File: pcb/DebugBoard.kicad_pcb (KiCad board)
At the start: 4 copper layers, 40 x 40 mm, 4 parts

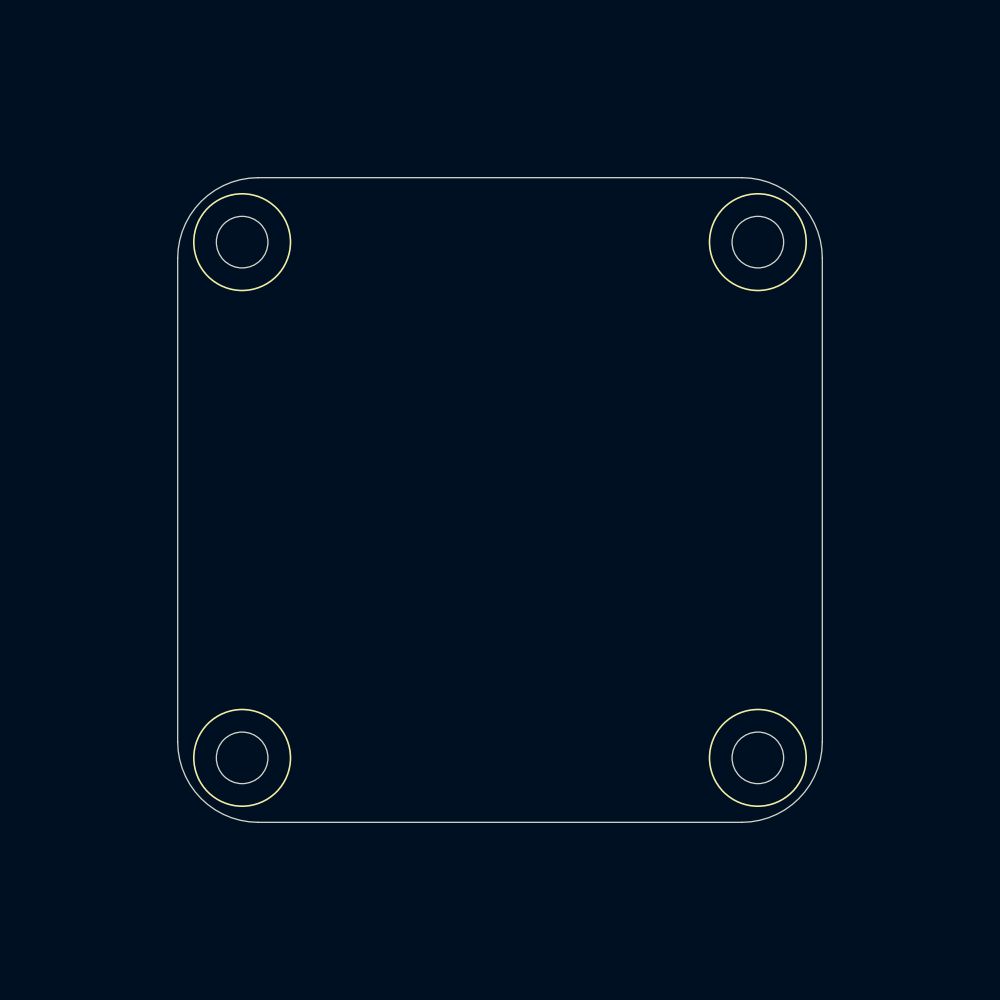
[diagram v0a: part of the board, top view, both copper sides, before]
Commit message: Basic expected components for `DebugBoard` PCB.
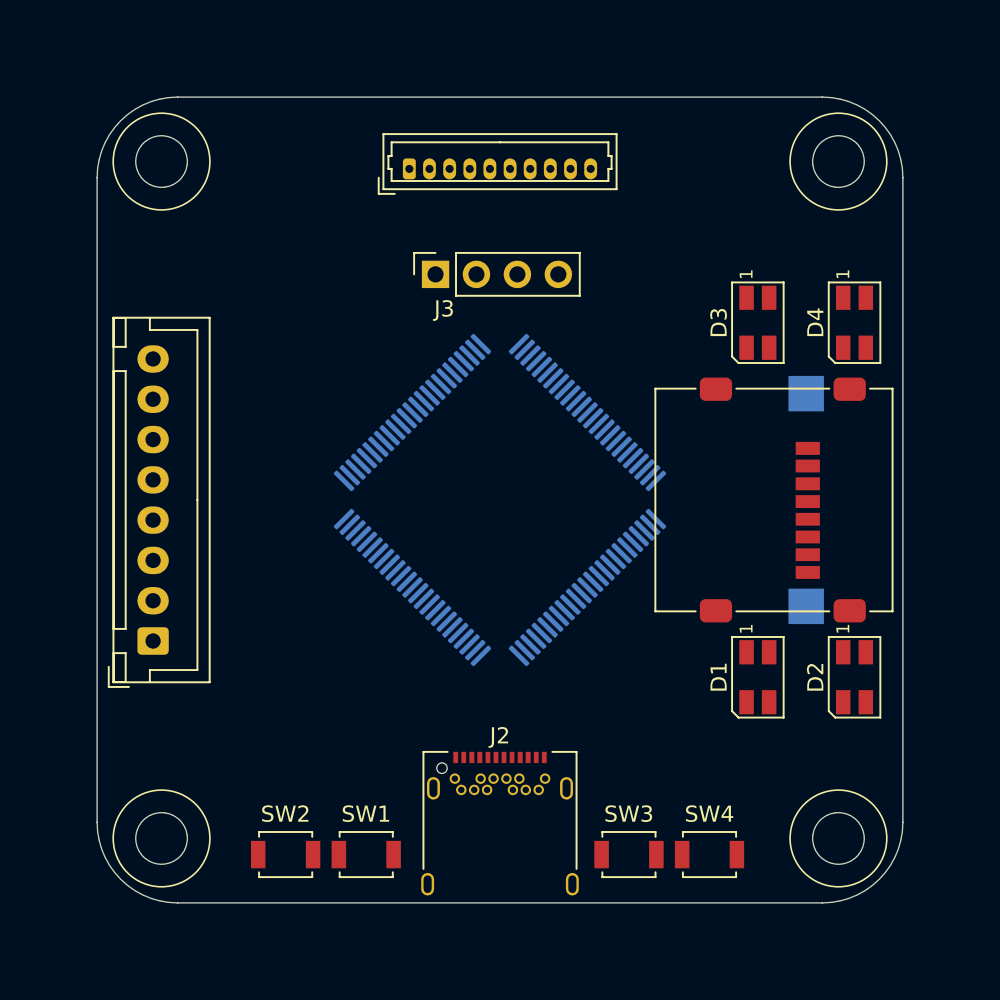
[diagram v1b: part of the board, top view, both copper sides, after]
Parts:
- added BZ1: AST1109MLTRQ, Buzzer_Beeper:Buzzer_Mallory_AST1109MLTRQ, B.Cu at (169.0, 100.0)
- added D1: 150141M173100, LED_SMD:LED_RGB_Wuerth-PLCC4_3.2x2.8mm_150141M173100, F.Cu at (166.0, 111.0)
- added D2: 150141M173100, LED_SMD:LED_RGB_Wuerth-PLCC4_3.2x2.8mm_150141M173100, F.Cu at (172.0, 111.0)
- added D3: 150141M173100, LED_SMD:LED_RGB_Wuerth-PLCC4_3.2x2.8mm_150141M173100, F.Cu at (166.0, 89.0)
- added D4: 150141M173100, LED_SMD:LED_RGB_Wuerth-PLCC4_3.2x2.8mm_150141M173100, F.Cu at (172.0, 89.0)
- added J1: Debug, pcb:Molex_PicoBlade_53047-1010_1x10_P1.25mm_Vertical, F.Cu at (144.4, 79.5)
- added J2: USB_C_Receptacle, pcb:USB_C_Receptacle_Amphenol_12401548E4-2A, F.Cu at (150.0, 121.0)
- added J3: Conn_01x04, pcb:SSD1306_Module_Connector, F.Cu at (146.0, 86.0)
- added J4: B8B-XH-A, Connector_JST:JST_XH_B8B-XH-A_1x08_P2.50mm_Vertical, F.Cu at (128.5, 108.8)
- added J5: 0472192001, pcb:microSD_HC_Molex_47219-2001, F.Cu at (167.0, 100.0)
- added SW1: B3U-1000P, Button_Switch_SMD:SW_SPST_B3U-1000P, F.Cu at (141.7, 122.0)
- added SW2: B3U-1000P, Button_Switch_SMD:SW_SPST_B3U-1000P, F.Cu at (136.7, 122.0)
- added SW3: B3U-1000P, Button_Switch_SMD:SW_SPST_B3U-1000P, F.Cu at (158.0, 122.0)
- added SW4: B3U-1000P, Button_Switch_SMD:SW_SPST_B3U-1000P, F.Cu at (163.0, 122.0)
- added U1: STM32H533VET6, Package_QFP:LQFP-100_14x14mm_P0.5mm, B.Cu at (150.0, 100.0)
- moved H1 7.07 mm to (129.0, 121.0)
- moved H2 7.07 mm to (171.0, 79.0)
- moved H3 7.07 mm to (129.0, 79.0)
- moved H4 7.07 mm to (171.0, 121.0)
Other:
- board size 40 x 40 mm -> 50 x 50 mm

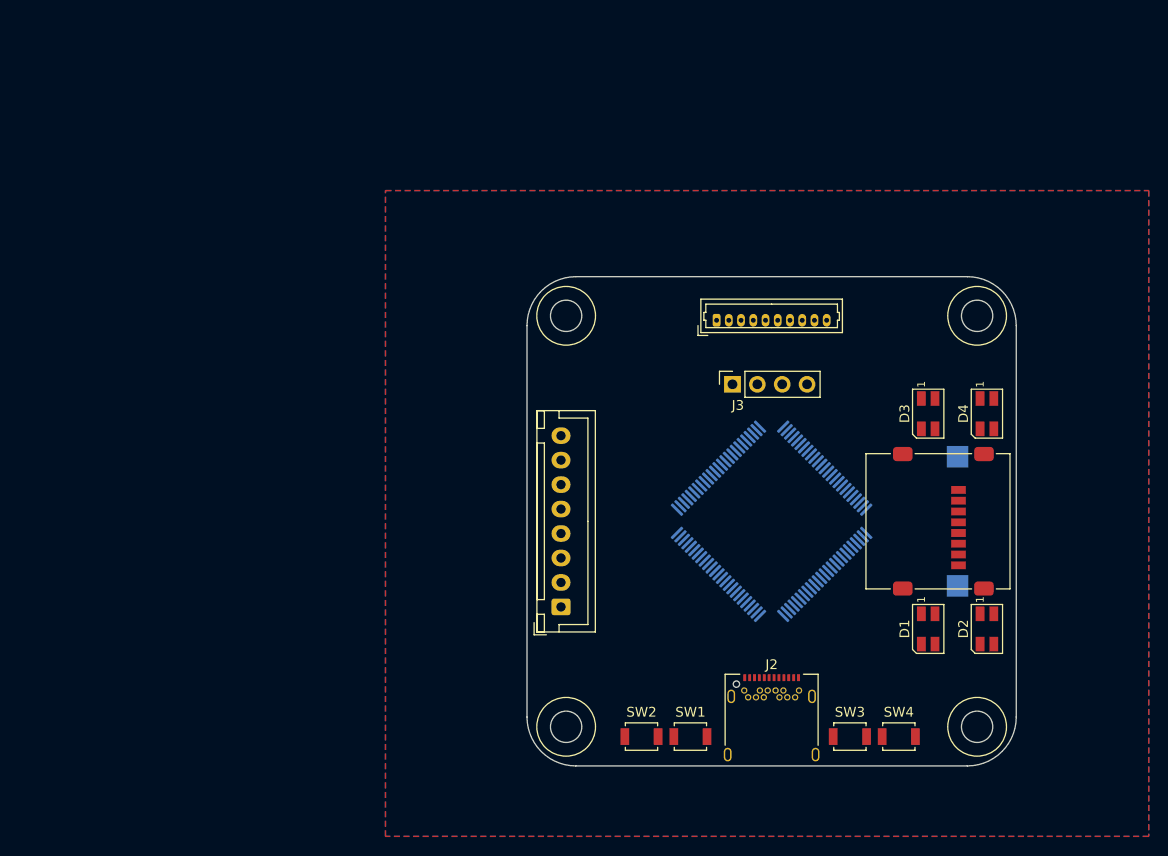
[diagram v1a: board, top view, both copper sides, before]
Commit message: Worked out uSD connector and debug LEDs details for `DebugBoard`.
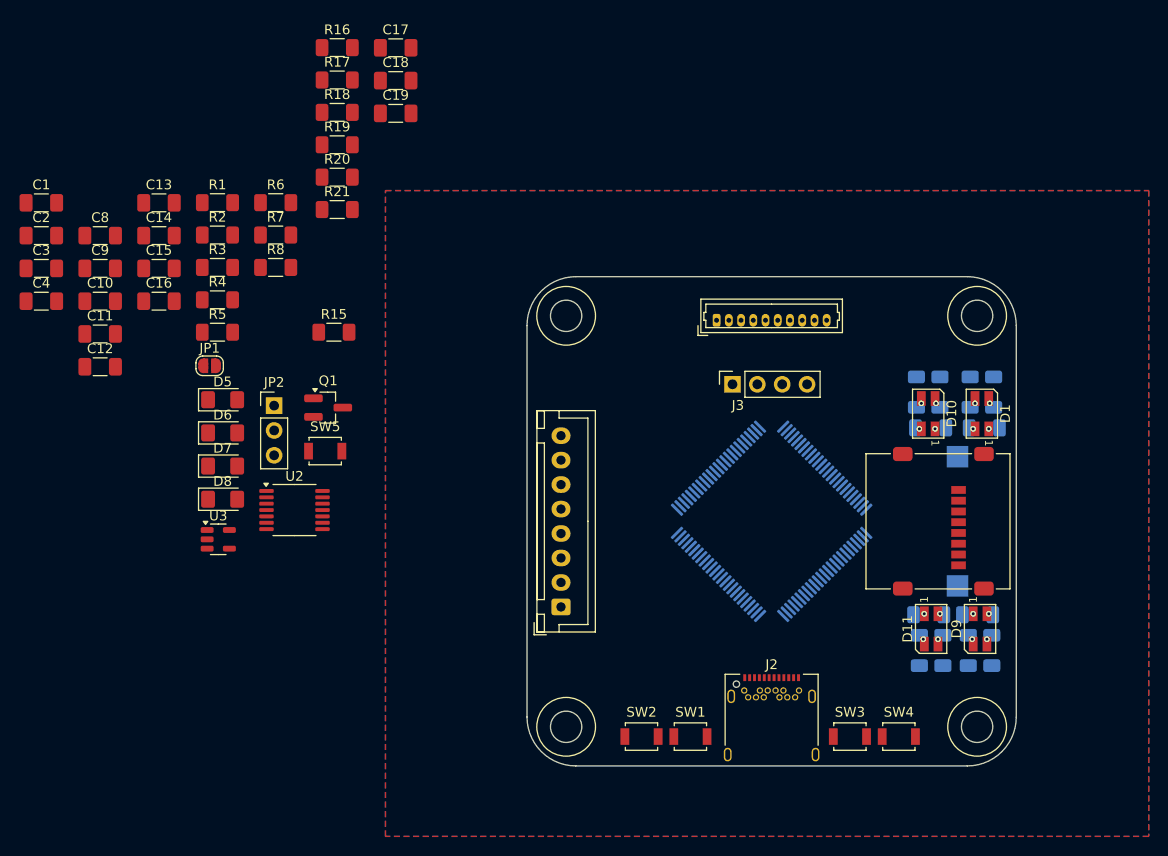
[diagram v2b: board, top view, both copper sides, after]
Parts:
- removed D2, D3, D4: 150141M173100, LED_SMD:LED_RGB_Wuerth-PLCC4_3.2x2.8mm_150141M173100
- added C1: 10u, Capacitor_SMD:C_1206_3216Metric_Pad1.33x1.80mm_HandSolder, F.Cu at (75.4, 67.5)
- added C10: 100n, Capacitor_SMD:C_1206_3216Metric_Pad1.33x1.80mm_HandSolder, F.Cu at (81.4, 77.5)
- added C11: 100n, Capacitor_SMD:C_1206_3216Metric_Pad1.33x1.80mm_HandSolder, F.Cu at (81.4, 80.9)
- added C12: 100n, Capacitor_SMD:C_1206_3216Metric_Pad1.33x1.80mm_HandSolder, F.Cu at (81.4, 84.2)
- added C13: 100n, Capacitor_SMD:C_1206_3216Metric_Pad1.33x1.80mm_HandSolder, F.Cu at (87.4, 67.5)
- added C14: 100n, Capacitor_SMD:C_1206_3216Metric_Pad1.33x1.80mm_HandSolder, F.Cu at (87.4, 70.8)
- added C15: 2u2, Capacitor_SMD:C_1206_3216Metric_Pad1.33x1.80mm_HandSolder, F.Cu at (87.4, 74.2)
- added C16: 2u2, Capacitor_SMD:C_1206_3216Metric_Pad1.33x1.80mm_HandSolder, F.Cu at (87.4, 77.5)
- added C17: 1u, Capacitor_SMD:C_1206_3216Metric_Pad1.33x1.80mm_HandSolder, F.Cu at (111.6, 51.6)
- added C18: 100n, Capacitor_SMD:C_1206_3216Metric_Pad1.33x1.80mm_HandSolder, F.Cu at (111.6, 55.0)
- added C19: 10n, Capacitor_SMD:C_1206_3216Metric_Pad1.33x1.80mm_HandSolder, F.Cu at (111.6, 58.3)
- added C2: 1u, Capacitor_SMD:C_1206_3216Metric_Pad1.33x1.80mm_HandSolder, F.Cu at (75.4, 70.8)
- added C3: 1u, Capacitor_SMD:C_1206_3216Metric_Pad1.33x1.80mm_HandSolder, F.Cu at (75.4, 74.2)
- added C4: 100n, Capacitor_SMD:C_1206_3216Metric_Pad1.33x1.80mm_HandSolder, F.Cu at (75.4, 77.5)
- added C8: 4u7, Capacitor_SMD:C_1206_3216Metric_Pad1.33x1.80mm_HandSolder, F.Cu at (81.4, 70.8)
- added C9: 100n, Capacitor_SMD:C_1206_3216Metric_Pad1.33x1.80mm_HandSolder, F.Cu at (81.4, 74.2)
- added D10: 150141M173100, LED_SMD:LED_RGB_Wuerth-PLCC4_3.2x2.8mm_150141M173100, F.Cu at (166.0, 89.0)
- added D11: 150141M173100, LED_SMD:LED_RGB_Wuerth-PLCC4_3.2x2.8mm_150141M173100, F.Cu at (166.3, 111.0)
- added D5: GREEN, LED_SMD:LED_1206_3216Metric_Pad1.42x1.75mm_HandSolder, F.Cu at (93.9, 87.6)
- added D6: GREEN, LED_SMD:LED_1206_3216Metric_Pad1.42x1.75mm_HandSolder, F.Cu at (93.9, 91.0)
- added D7: RED, LED_SMD:LED_1206_3216Metric_Pad1.42x1.75mm_HandSolder, F.Cu at (93.9, 94.4)
- added D8: GREEN, LED_SMD:LED_1206_3216Metric_Pad1.42x1.75mm_HandSolder, F.Cu at (93.9, 97.7)
- added D9: 150141M173100, LED_SMD:LED_RGB_Wuerth-PLCC4_3.2x2.8mm_150141M173100, F.Cu at (171.3, 111.0)
- added JP1: SolderJumper_2_Open, Jumper:SolderJumper-2_P1.3mm_Open_RoundedPad1.0x1.5mm, F.Cu at (92.6, 84.1)
- added JP2: Jumper_3_Bridged12, Connector_PinHeader_2.54mm:PinHeader_1x03_P2.54mm_Vertical, F.Cu at (99.2, 88.2)
- added Q1: S8050, Package_TO_SOT_SMD:SOT-23_Handsoldering, F.Cu at (104.7, 88.4)
- added R1: 5k1, Resistor_SMD:R_1206_3216Metric_Pad1.30x1.75mm_HandSolder, F.Cu at (93.4, 67.4)
- added R10: 6k8, Resistor_SMD:R_1206_3216Metric_Pad1.30x1.75mm_HandSolder, B.Cu at (170.3, 86.8)
- added R11: 6k8, Resistor_SMD:R_1206_3216Metric_Pad1.30x1.75mm_HandSolder, B.Cu at (171.7, 90.5)
- added R12: 6k8, Resistor_SMD:R_1206_3216Metric_Pad1.30x1.75mm_HandSolder, B.Cu at (170.1, 113.2)
- added R13: 6k8, Resistor_SMD:R_1206_3216Metric_Pad1.30x1.75mm_HandSolder, B.Cu at (172.5, 113.2)
- added R14: 6k8, Resistor_SMD:R_1206_3216Metric_Pad1.30x1.75mm_HandSolder, B.Cu at (171.0, 109.5)
- added R15: 47k, Resistor_SMD:R_1206_3216Metric_Pad1.30x1.75mm_HandSolder, F.Cu at (105.3, 80.7)
- added R16: R_Small, Resistor_SMD:R_1206_3216Metric_Pad1.30x1.75mm_HandSolder, F.Cu at (105.6, 51.6)
- added R17: R_Small, Resistor_SMD:R_1206_3216Metric_Pad1.30x1.75mm_HandSolder, F.Cu at (105.6, 54.9)
- added R18: R_Small, Resistor_SMD:R_1206_3216Metric_Pad1.30x1.75mm_HandSolder, F.Cu at (105.6, 58.2)
- added R19: R_Small, Resistor_SMD:R_1206_3216Metric_Pad1.30x1.75mm_HandSolder, F.Cu at (105.6, 61.5)
- added R2: 4K, Resistor_SMD:R_1206_3216Metric_Pad1.30x1.75mm_HandSolder, F.Cu at (93.4, 70.7)
- added R20: R_Small, Resistor_SMD:R_1206_3216Metric_Pad1.30x1.75mm_HandSolder, F.Cu at (105.6, 64.8)
- added R21: R_Small, Resistor_SMD:R_1206_3216Metric_Pad1.30x1.75mm_HandSolder, F.Cu at (105.6, 68.1)
- added R22: 6k8, Resistor_SMD:R_1206_3216Metric_Pad1.30x1.75mm_HandSolder, B.Cu at (167.2, 86.8)
- added R23: 6k8, Resistor_SMD:R_1206_3216Metric_Pad1.30x1.75mm_HandSolder, B.Cu at (164.8, 86.8)
- added R24: 6k8, Resistor_SMD:R_1206_3216Metric_Pad1.30x1.75mm_HandSolder, B.Cu at (166.3, 90.5)
- added R25: 6k8, Resistor_SMD:R_1206_3216Metric_Pad1.30x1.75mm_HandSolder, B.Cu at (165.1, 113.2)
- added R26: 6k8, Resistor_SMD:R_1206_3216Metric_Pad1.30x1.75mm_HandSolder, B.Cu at (167.5, 113.2)
- added R27: 6k8, Resistor_SMD:R_1206_3216Metric_Pad1.30x1.75mm_HandSolder, B.Cu at (166.0, 109.5)
- added R3: 10K, Resistor_SMD:R_1206_3216Metric_Pad1.30x1.75mm_HandSolder, F.Cu at (93.4, 74.1)
- added R4: 4K, Resistor_SMD:R_1206_3216Metric_Pad1.30x1.75mm_HandSolder, F.Cu at (93.4, 77.4)
- added R5: 2K, Resistor_SMD:R_1206_3216Metric_Pad1.30x1.75mm_HandSolder, F.Cu at (93.4, 80.7)
- added R6: 2K, Resistor_SMD:R_1206_3216Metric_Pad1.30x1.75mm_HandSolder, F.Cu at (99.3, 67.4)
- added R7: 50k, Resistor_SMD:R_1206_3216Metric_Pad1.30x1.75mm_HandSolder, F.Cu at (99.3, 70.7)
- added R8: 10k, Resistor_SMD:R_1206_3216Metric_Pad1.30x1.75mm_HandSolder, F.Cu at (99.3, 74.1)
- added R9: 6k8, Resistor_SMD:R_1206_3216Metric_Pad1.30x1.75mm_HandSolder, B.Cu at (172.7, 86.8)
- added SW5: B3U-1000P, Button_Switch_SMD:SW_SPST_B3U-1000P, F.Cu at (104.4, 92.8)
- added U2: MCP2221A-I/ST, Package_SO:TSSOP-14_4.4x5mm_P0.65mm, F.Cu at (101.2, 98.8)
- added U3: AP2112K-3.3, Package_TO_SOT_SMD:SOT-23-5, F.Cu at (93.4, 101.8)
- moved D1 22.7 mm to (171.5, 89.0), turned to -90 degrees
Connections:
- D1 pad 1: unconnected-(D1-A-Pad1) -> +3.3V
- D1 pad 2: unconnected-(D1-BK-Pad2) -> Net-(D1-BK)
- D1 pad 3: unconnected-(D1-RK-Pad3) -> Net-(D1-RK)
- D1 pad 4: unconnected-(D1-GK-Pad4) -> Net-(D1-GK)
- U1 pad 10: Net-(U1-VSS-Pad10) -> GND
- U1 pad 100: unconnected-(U1-VDD-Pad100) -> +3.3V
- U1 pad 11: unconnected-(U1-VDD-Pad11) -> +3.3V
- U1 pad 12: unconnected-(U1-PH0-Pad12) -> vn100_sync_out
- U1 pad 14: unconnected-(U1-NRST-Pad14) -> RESET
- U1 pad 15: unconnected-(U1-PC0-Pad15) -> led_channel_red
- U1 pad 16: unconnected-(U1-PC1-Pad16) -> led_channel_green
- U1 pad 17: unconnected-(U1-PC2-Pad17) -> openmv_spi_miso
- U1 pad 18: unconnected-(U1-PC3-Pad18) -> openmv_spi_mosi
- U1 pad 19: unconnected-(U1-VSSA-Pad19) -> GND
- U1 pad 20: unconnected-(U1-VREF--Pad20) -> GND
- U1 pad 21: unconnected-(U1-VREF+-Pad21) -> +3.3V
- U1 pad 22: unconnected-(U1-VDDA-Pad22) -> +3.3V
- U1 pad 23: unconnected-(U1-PA0-Pad23) -> led_channel_blue
- U1 pad 25: unconnected-(U1-PA2-Pad25) -> stlink_tx
- U1 pad 26: unconnected-(U1-PA3-Pad26) -> stlink_rx
- U1 pad 27: Net-(U1-VSS-Pad10) -> GND
- U1 pad 28: unconnected-(U1-VDD-Pad28) -> +3.3V
- U1 pad 29: unconnected-(U1-PA4-Pad29) -> motor_disable
- U1 pad 30: unconnected-(U1-PA5-Pad30) -> buzzer
- U1 pad 34: unconnected-(U1-PC5-Pad34) -> vn100_sync_in
- U1 pad 35: unconnected-(U1-PB0-Pad35) -> esp32_spi_miso
- U1 pad 36: unconnected-(U1-PB1-Pad36) -> esp32_spi_clock
- U1 pad 37: unconnected-(U1-PB2-Pad37) -> openmv_reset
- U1 pad 39: unconnected-(U1-PE8-Pad39) -> esp32_reset
- U1 pad 4: unconnected-(U1-PE5-Pad4) -> motor_step_z
- U1 pad 40: unconnected-(U1-PE9-Pad40) -> motor_step_x
- U1 pad 41: unconnected-(U1-PE10-Pad41) -> serial_reset
- U1 pad 47: unconnected-(U1-PB10-Pad47) -> openmv_spi_clock
- U1 pad 48: unconnected-(U1-VCAP-Pad48) -> VCAP
- U1 pad 49: Net-(U1-VSS-Pad10) -> GND
- U1 pad 50: unconnected-(U1-VDD-Pad50) -> +3.3V
- U1 pad 51: unconnected-(U1-PB12-Pad51) -> openmv_spi_nss
- U1 pad 53: unconnected-(U1-PB14-Pad53) -> motor_uart_tx
- U1 pad 54: unconnected-(U1-PB15-Pad54) -> motor_uart_rx
- U1 pad 55: unconnected-(U1-PD8-Pad55) -> vn100_uart_tx
- U1 pad 56: unconnected-(U1-PD9-Pad56) -> vn100_uart_rx
- U1 pad 58: unconnected-(U1-PD11-Pad58) -> serial_rx
- U1 pad 59: unconnected-(U1-PD12-Pad59) -> serial_tx
- U1 pad 6: unconnected-(U1-VBAT-Pad6) -> +3.3V
- U1 pad 60: unconnected-(U1-PD13-Pad60) -> lsm6dsv32x_interrupt_1
- U1 pad 61: unconnected-(U1-PD14-Pad61) -> lsm6dsv32x_interrupt_2
- U1 pad 62: unconnected-(U1-PD15-Pad62) -> lsm6dsv32x_chip_select
- U1 pad 63: unconnected-(U1-PC6-Pad63) -> motor_step_y
- U1 pad 65: unconnected-(U1-PC8-Pad65) -> sd_data_0
- U1 pad 66: unconnected-(U1-PC9-Pad66) -> sd_data_1
- U1 pad 67: unconnected-(U1-PA8-Pad67) -> motor_direction_y
- U1 pad 68: unconnected-(U1-PA9-Pad68) -> motor_direction_x
- U1 pad 69: unconnected-(U1-PA10-Pad69) -> motor_direction_z
- U1 pad 7: unconnected-(U1-PC13-Pad7) -> vn100_tare_restore
- U1 pad 72: unconnected-(U1-PA13(JTMS-Pad72) -> swdio
- U1 pad 73: unconnected-(U1-VDDUSB-Pad73) -> +3.3V
- U1 pad 74: Net-(U1-VSS-Pad10) -> GND
- U1 pad 75: unconnected-(U1-VDD-Pad75) -> +3.3V
- U1 pad 76: unconnected-(U1-PA14(JTCK-Pad76) -> swclk
- U1 pad 78: unconnected-(U1-PC10-Pad78) -> sd_data_2
- U1 pad 79: unconnected-(U1-PC11-Pad79) -> sd_data_3
- U1 pad 80: unconnected-(U1-PC12-Pad80) -> sd_clock
- U1 pad 81: unconnected-(U1-PD0-Pad81) -> battery_allowed
- U1 pad 82: unconnected-(U1-PD1-Pad82) -> external_detected
- U1 pad 83: unconnected-(U1-PD2-Pad83) -> sd_cmd
- U1 pad 86: unconnected-(U1-PD5-Pad86) -> openmv_spi_ready
- U1 pad 87: unconnected-(U1-PD6-Pad87) -> vehicle_interface_i2c_clock
- U1 pad 88: unconnected-(U1-PD7-Pad88) -> vehicle_interface_i2c_data
- U1 pad 89: unconnected-(U1-PB3(JTDO-Pad89) -> swo
- U1 pad 9: unconnected-(U1-PC15-Pad9) -> lis2mdl_chip_select
- U1 pad 90: unconnected-(U1-PB4(NJTRST)-Pad90) -> lis2mdl_data_ready
- U1 pad 91: unconnected-(U1-PB5-Pad91) -> esp32_spi_mosi
- U1 pad 92: unconnected-(U1-PB6-Pad92) -> sensor_i2c_clock
- U1 pad 93: unconnected-(U1-PB7-Pad93) -> sensor_i2c_data
- U1 pad 94: unconnected-(U1-BOOT0-Pad94) -> BOOT0
- U1 pad 95: unconnected-(U1-PB8-Pad95) -> esp32_spi_nss
- U1 pad 97: unconnected-(U1-PE0-Pad97) -> esp32_spi_ready
- U1 pad 98: unconnected-(U1-VCAP-Pad98) -> VCAP
- U1 pad 99: Net-(U1-VSS-Pad10) -> GND
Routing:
- net Net-(D9-RK): vias 0 -> 1
- net Net-(D9-GK): vias 0 -> 1
- net Net-(D9-BK): vias 0 -> 1
- net Net-(D11-RK): vias 0 -> 1
- net Net-(D11-GK): vias 0 -> 1
- net Net-(D11-BK): vias 0 -> 1
- net Net-(D10-RK): vias 0 -> 1
- net Net-(D10-GK): vias 0 -> 1
- net Net-(D10-BK): vias 0 -> 1
- net Net-(D1-RK): vias 0 -> 1
- net Net-(D1-GK): vias 0 -> 1
- net Net-(D1-BK): vias 0 -> 1
- net +3.3V: vias 0 -> 4

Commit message: Added buttons and updated MCU pin-outs for `DebugBoard`.
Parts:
- removed SW3, SW4: B3U-1000P, Button_Switch_SMD:SW_SPST_B3U-1000P
- added R28: 6k8, Resistor_SMD:R_1206_3216Metric_Pad1.30x1.75mm_HandSolder, B.Cu at (164.8, 119.5)
- added R29: 6k8, Resistor_SMD:R_1206_3216Metric_Pad1.30x1.75mm_HandSolder, B.Cu at (164.8, 122.8)
- J2: value USB_C_Receptacle -> 12401598E4_2A; footprint pcb:USB_C_Receptacle_Amphenol_12401548E4-2A -> pcb:AMPHENOL_12401598E4_2A
- moved R1 45.2 mm to (101.0, 112.0)
- moved SW2 28.2 mm to (164.8, 119.5)
- moved SW1 23.1 mm to (164.8, 122.8)
- moved J2 4.84 mm to (150.0, 116.2)
- renumbered D5 to D2, D6 to D3, D7 to D4, D8 to D5
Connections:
- J2 pad A6: Net-(U2-D-) -> Net-(J2-DP1)
- J2 pad A7: Net-(U2-D+) -> Net-(J2-DN1)
- J2 pad B6: Net-(U2-D-) -> Net-(J2-DP1)
- J2 pad B7: Net-(U2-D+) -> Net-(J2-DN1)
- J4 pad 1: +3.3V -> GND
- J4 pad 2: debug_i2c_data -> +3.3V
- J4 pad 3: debug_i2c_clock -> unconnected-(J4-Pin_3-Pad3)
- J4 pad 4: unconnected-(J4-Pin_4-Pad4) -> debug_i2c_data
- J4 pad 5: unconnected-(J4-Pin_5-Pad5) -> debug_i2c_clock
- J4 pad 7: unconnected-(J4-Pin_7-Pad7) -> +3.3V
- SW1 pad 1: unconnected-(SW1-Pad1) -> button_B
- SW1 pad 2: unconnected-(SW1-Pad2) -> Net-(R29-Pad2)
- SW2 pad 1: unconnected-(SW2-Pad1) -> button_A
- SW2 pad 2: unconnected-(SW2-Pad2) -> Net-(R28-Pad2)
- U1 pad 1: unconnected-(U1-PE2-Pad1) -> led_green_B
- U1 pad 12: vn100_sync_out -> unconnected-(U1-PH0-Pad12)
- U1 pad 15: led_channel_red -> unconnected-(U1-PC0-Pad15)
- U1 pad 16: led_channel_green -> unconnected-(U1-PC1-Pad16)
- U1 pad 17: openmv_spi_miso -> unconnected-(U1-PC2-Pad17)
- U1 pad 18: openmv_spi_mosi -> unconnected-(U1-PC3-Pad18)
- U1 pad 2: unconnected-(U1-PE3-Pad2) -> led_blue_B
- U1 pad 23: led_channel_blue -> unconnected-(U1-PA0-Pad23)
- U1 pad 29: motor_disable -> unconnected-(U1-PA4-Pad29)
- U1 pad 3: unconnected-(U1-PE4-Pad3) -> led_red_C
- U1 pad 34: vn100_sync_in -> unconnected-(U1-PC5-Pad34)
- U1 pad 35: esp32_spi_miso -> unconnected-(U1-PB0-Pad35)
- U1 pad 36: esp32_spi_clock -> unconnected-(U1-PB1-Pad36)
- U1 pad 37: openmv_reset -> unconnected-(U1-PB2-Pad37)
- U1 pad 38: unconnected-(U1-PE7-Pad38) -> led_red_D
- U1 pad 39: esp32_reset -> led_green_D
- U1 pad 4: motor_step_z -> led_green_C
- U1 pad 40: motor_step_x -> led_blue_D
- U1 pad 42: unconnected-(U1-PE11-Pad42) -> button_A
- U1 pad 43: unconnected-(U1-PE12-Pad43) -> button_B
- U1 pad 47: openmv_spi_clock -> unconnected-(U1-PB10-Pad47)
- U1 pad 5: unconnected-(U1-PE6-Pad5) -> led_blue_C
- U1 pad 51: openmv_spi_nss -> unconnected-(U1-PB12-Pad51)
- U1 pad 53: motor_uart_tx -> unconnected-(U1-PB14-Pad53)
- U1 pad 54: motor_uart_rx -> unconnected-(U1-PB15-Pad54)
- U1 pad 55: vn100_uart_tx -> unconnected-(U1-PD8-Pad55)
- U1 pad 56: vn100_uart_rx -> unconnected-(U1-PD9-Pad56)
- U1 pad 60: lsm6dsv32x_interrupt_1 -> unconnected-(U1-PD13-Pad60)
- U1 pad 61: lsm6dsv32x_interrupt_2 -> unconnected-(U1-PD14-Pad61)
- U1 pad 62: lsm6dsv32x_chip_select -> unconnected-(U1-PD15-Pad62)
- U1 pad 63: motor_step_y -> unconnected-(U1-PC6-Pad63)
- U1 pad 67: motor_direction_y -> unconnected-(U1-PA8-Pad67)
- U1 pad 68: motor_direction_x -> led_red_A
- U1 pad 69: motor_direction_z -> led_green_A
- U1 pad 7: vn100_tare_restore -> unconnected-(U1-PC13-Pad7)
- U1 pad 70: unconnected-(U1-PA11-Pad70) -> led_blue_A
- U1 pad 81: battery_allowed -> unconnected-(U1-PD0-Pad81)
- U1 pad 82: external_detected -> unconnected-(U1-PD1-Pad82)
- U1 pad 86: openmv_spi_ready -> unconnected-(U1-PD5-Pad86)
- U1 pad 87: vehicle_interface_i2c_clock -> display_i2c_clock
- U1 pad 88: vehicle_interface_i2c_data -> display_i2c_data
- U1 pad 9: lis2mdl_chip_select -> unconnected-(U1-PC15-Pad9)
- U1 pad 90: lis2mdl_data_ready -> unconnected-(U1-PB4(NJTRST)-Pad90)
- U1 pad 91: esp32_spi_mosi -> unconnected-(U1-PB5-Pad91)
- U1 pad 92: sensor_i2c_clock -> debug_i2c_clock
- U1 pad 93: sensor_i2c_data -> debug_i2c_data
- U1 pad 95: esp32_spi_nss -> unconnected-(U1-PB8-Pad95)
- U1 pad 97: esp32_spi_ready -> led_red_B
- U2 pad 12: Net-(U2-D-) -> Net-(J2-DN1)
- U2 pad 13: Net-(U2-D+) -> Net-(J2-DP1)
